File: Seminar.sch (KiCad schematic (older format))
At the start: 0 parts

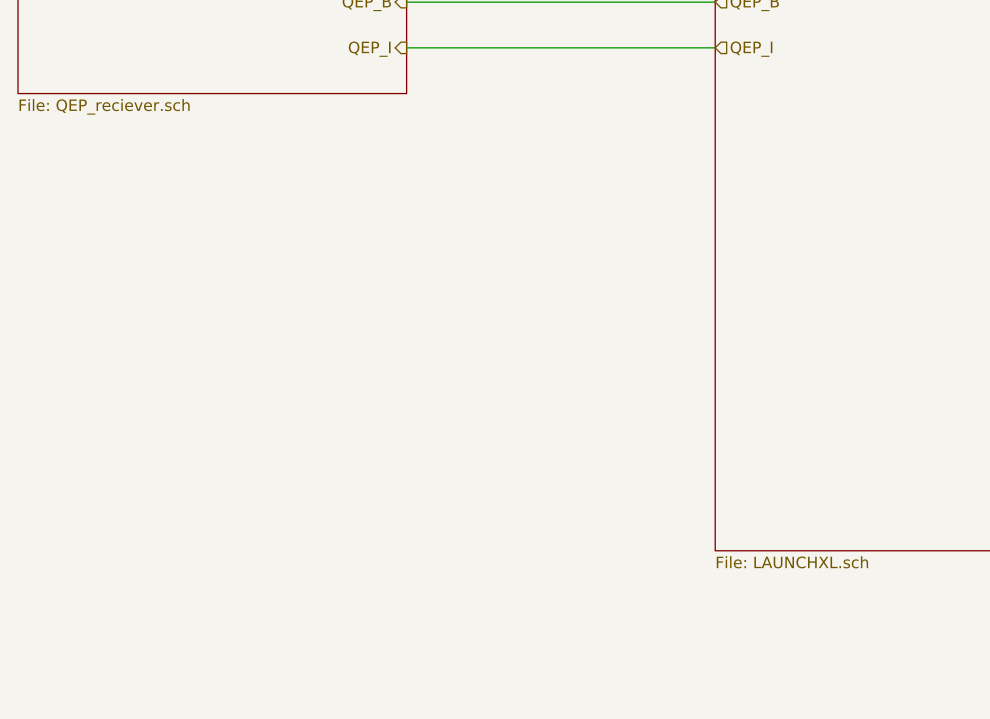
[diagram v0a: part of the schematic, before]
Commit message: Naredil še sheet napajanje in popravil merilnik napetosti pri merjenju fazne napetosti
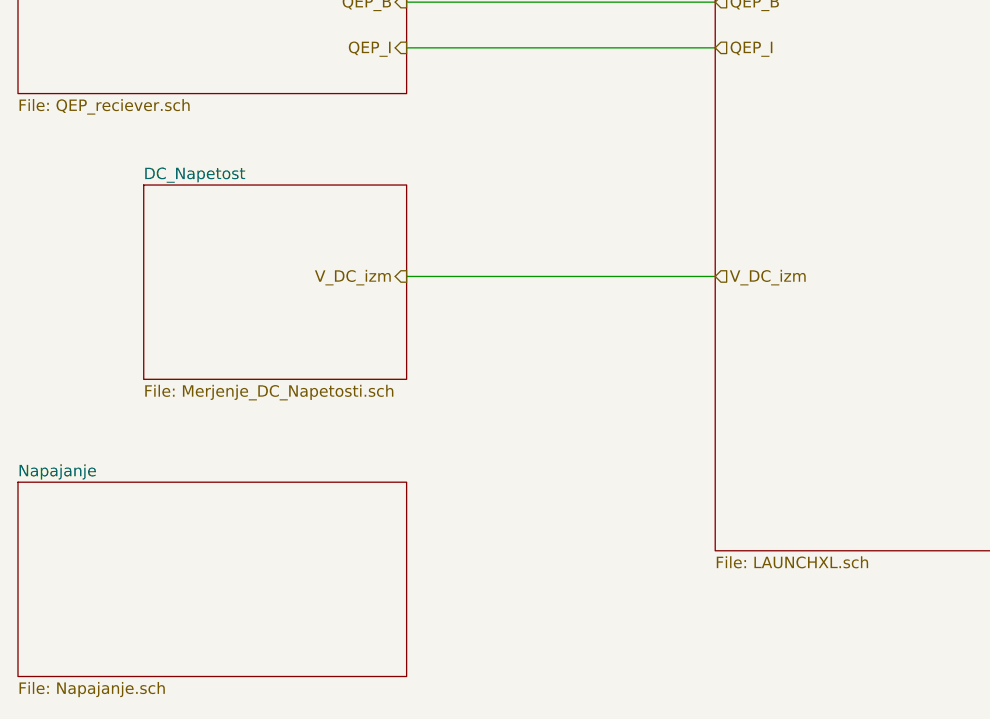
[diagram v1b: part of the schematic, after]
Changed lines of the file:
@@
 $Descr A4 11693 8268
 encoding utf-8
-Sheet 1 7
+Sheet 1 9
 Title ""
 Date ""
@@
 Wire Wire Line
 	10500 1550 10800 1550
+$Sheet
+S 1900 4200 1150 850
+U 5BD3A78C
+F0 "DC_Napetost" 50
+F1 "Merjenje_DC_Napetosti.sch" 50
+$EndSheet
+Text HLabel 3050 4600 0    50   Output ~ 0
+V_DC_izm
+Text HLabel 4400 4600 2    50   Input ~ 0
+V_DC_izm
+Wire Wire Line
+	3050 4600 4400 4600
+$Sheet
+S 1350 5500 1700 850
+U 5BD7DC9C
+F0 "Napajanje" 50
+F1 "Napajanje.sch" 50
+$EndSheet
 $EndSCHEMATC
